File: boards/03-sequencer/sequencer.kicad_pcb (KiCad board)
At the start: 4 copper layers, 245 x 255 mm, 2008 parts, among them J1 BUS, J2 LINK, Q1 2N7000, Q10 2N7000, Q100 2N7000, Q101 2N7000, Q102 2N7000, Q103 2N7000, Q104 2N7000, Q105 2N7000, Q106 2N7000, Q107 2N7000, Q108 2N7000, Q109 2N7000, Q11 2N7000, Q110 2N7000, Q111 2N7000, Q112 2N7000, Q113 2N7000, Q114 2N7000, Q115 2N7000, Q116 2N7000, Q117 2N7000, Q118 2N7000, Q119 2N7000, Q12 2N7000, Q120 2N7000, Q121 2N7000, Q122 2N7000, Q123 2N7000, Q124 2N7000, Q125 2N7000, Q126 2N7000, Q127 2N7000, Q128 2N7000, Q129 2N7000, Q13 2N7000, Q130 2N7000, Q131 2N7000, Q132 2N7000, Q133 2N7000, Q134 2N7000, Q135 2N7000, Q136 2N7000, Q137 2N7000, Q138 2N7000, Q139 2N7000, Q14 2N7000, Q140 2N7000, Q141 2N7000, Q142 2N7000, Q143 2N7000, Q144 2N7000, Q145 2N7000, Q146 2N7000, Q147 2N7000, Q148 2N7000, Q149 2N7000, Q15 2N7000, Q150 2N7000, Q151 2N7000, Q152 2N7000, Q153 2N7000, Q154 2N7000, Q155 2N7000, Q156 2N7000, Q157 2N7000, Q158 2N7000, Q159 2N7000, Q16 2N7000, Q160 2N7000, Q161 2N7000, Q162 2N7000, Q163 2N7000, Q164 2N7000, Q165 2N7000, Q166 2N7000, Q167 2N7000, Q168 2N7000, Q169 2N7000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

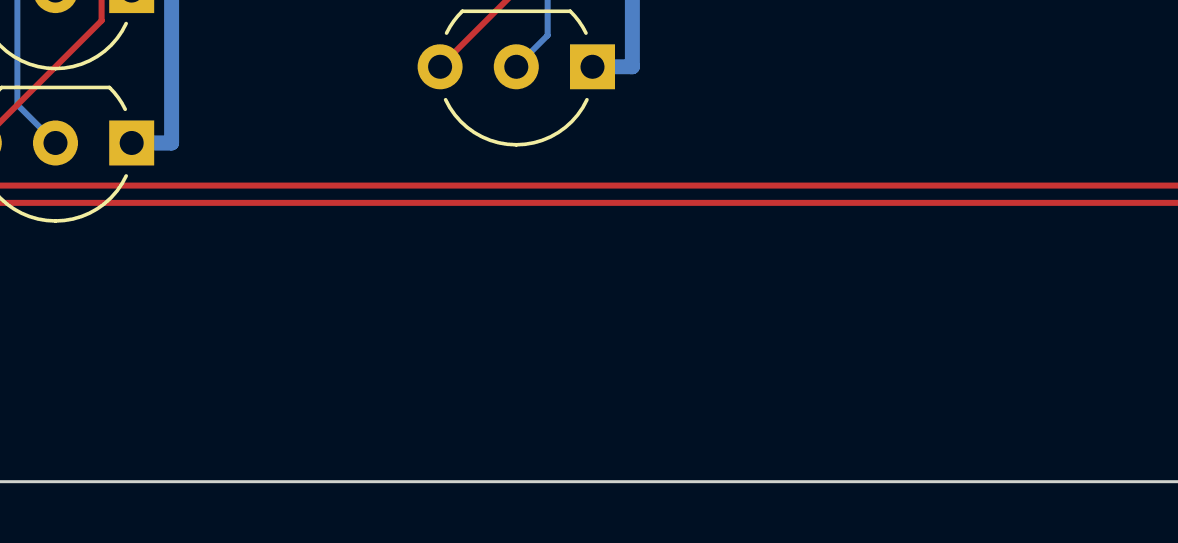
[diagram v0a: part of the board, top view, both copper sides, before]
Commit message: The Nibble logo on the front silkscreen of every board
lib/logo/nibble.png traced by sim/logo.py (potracer) into two silkscreen
footprints, lib/nibble.pretty/Logo_Nibble (icon and word, 27 x 8 mm) and
Logo_Nibble_Icon (8 x 8): filled polygons, holes slit in. At 8 mm the
ribbon's lines print 0.39 mm wide and 0.24 mm apart; the fab's minimum
is 0.15. No pads, no copper, out of the parts list and the position file.

pcb.py places it on every board before the labels are fitted
(place_logo): icon and word where a patch 27 x 8 mm is free of pads,
vias, outlines, courtyards, the labels and 1 mm of edge, the icon alone
otherwise, the nearest such patch to the board's name; the fitter then
keeps the labels off it. 25 boards took the full logo, the coupon the
icon. All 26 re-silked in place (no re-route, the schematics untouched).
The order gate wants exactly one logo on a board; bom.py counts it as no
part. Two pcbnew quirks met on the way: a footprint removed in the
fitter's process makes the next loaded board untyped (every hidden
reference became an obstacle and BUS0 on the hub fell back to 0.8 mm),
and after a text is removed the footprints are untyped too, so resilk
takes the old logo off before the texts.

Gate all pass on all 26, every builder writes what is committed, parts
tables unchanged. The pilot's three zips are new again (order-1.md).

Co-Authored-By: Claude Fable 5.1 <noreply@anthropic.com>
Claude-Session: https://claude.ai/code/session_01RktbhdQjDu7SpFpvkevyUU
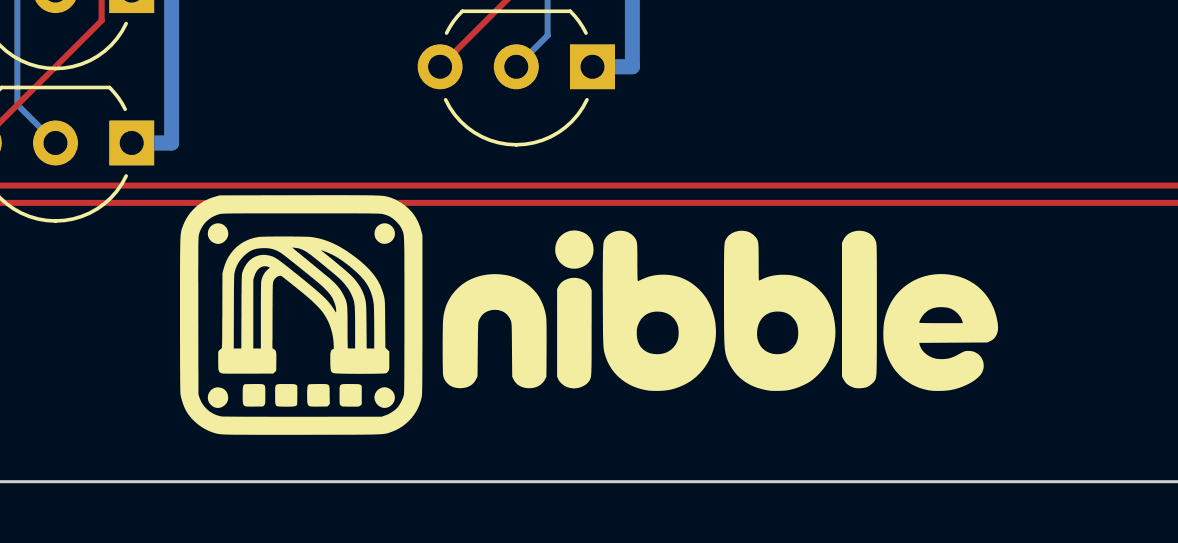
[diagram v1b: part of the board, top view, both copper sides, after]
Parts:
- added LOGO: Logo_Nibble, Logo_Nibble, F.Cu at (83.1, 249.4)
